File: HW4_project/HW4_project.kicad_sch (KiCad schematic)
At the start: 26 parts, among them J1 CP2102, J2 BATT, J3 L, J4 R, J5 SCO, SW1 MCLR, SW2 SW_SPDT, SW3 USER, U1 AP7381-33V, U2 PIC32

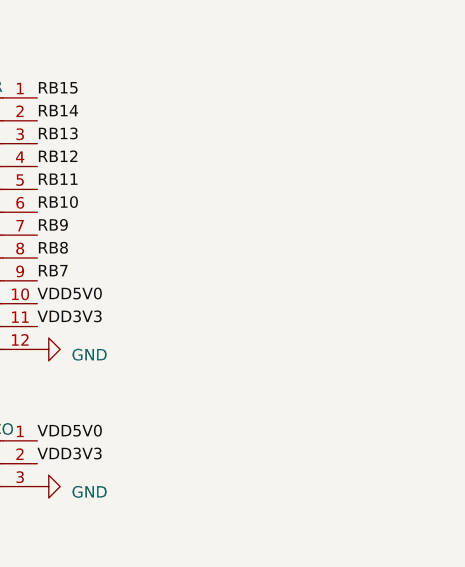
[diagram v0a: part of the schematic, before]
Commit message: HW4: silkscreen revisions
- added labels for all the broken-out pins
- fixed spacing on the button components
- added NURC logo
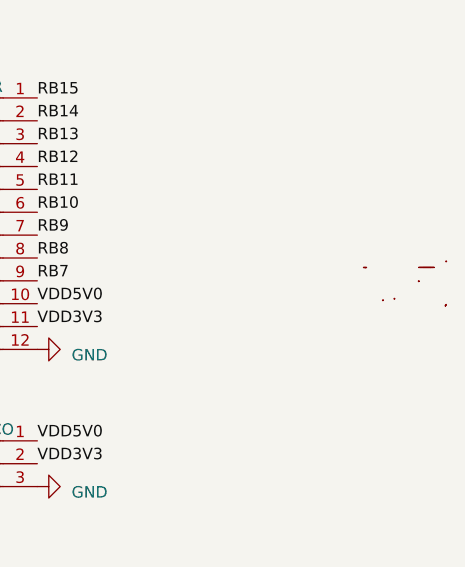
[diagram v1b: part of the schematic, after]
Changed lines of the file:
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@@
+    )
+  )
+  (symbol (lib_id "HW4_library:LOGO") (at 182.88 87.63 0) (unit 1)
+    (in_bom yes) (on_board yes) (dnp no) (fields_autoplaced)
+    (property "Reference" "#G1" (at 182.88 82.8463 0)
+      (effects (font (size 1.27 1.27)) hide)
+    )
+    (property "Value" "LOGO" (at 182.88 92.4137 0)
+      (effects (font (size 1.27 1.27)) hide)
+    )
+    (property "Footprint" "" (at 182.88 87.63 0)
+      (effects (font (size 1.27 1.27)) hide)
+    )
+    (property "Datasheet" "" (at 182.88 87.63 0)
+      (effects (font (size 1.27 1.27)) hide)
+    )
+    (instances
+      (project "HW4_project"
+        (path "/9c574890-de61-4ebc-b55b-dc483313a1fa"
+          (reference "#G1") (unit 1)
+        )
+      )
     )
   )
